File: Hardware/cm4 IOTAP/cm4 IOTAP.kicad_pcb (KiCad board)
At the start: 2 copper layers, 120 x 110 mm, 97 parts, among them IC1 TPS3700-WSON, J1 USB_C_Receptacle_USB2.0, K1 J104D2C3VDC.15S, Q1 AO3400A, U1 MAX15062A, U2 Compute_Module_4_Connectors, U3 PC817, U4 PC817, U5 PC817, U6 PC817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

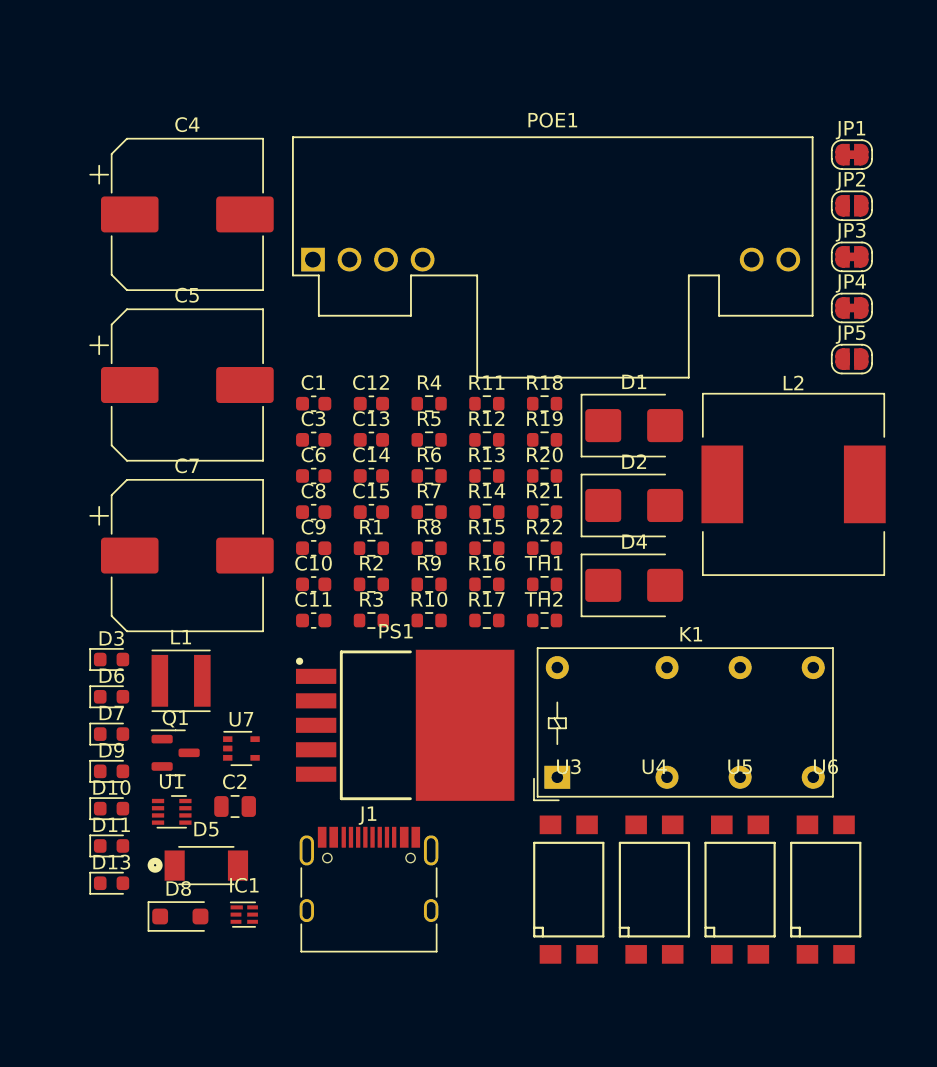
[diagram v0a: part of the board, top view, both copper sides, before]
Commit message: add resistors for Ethernet activity lights
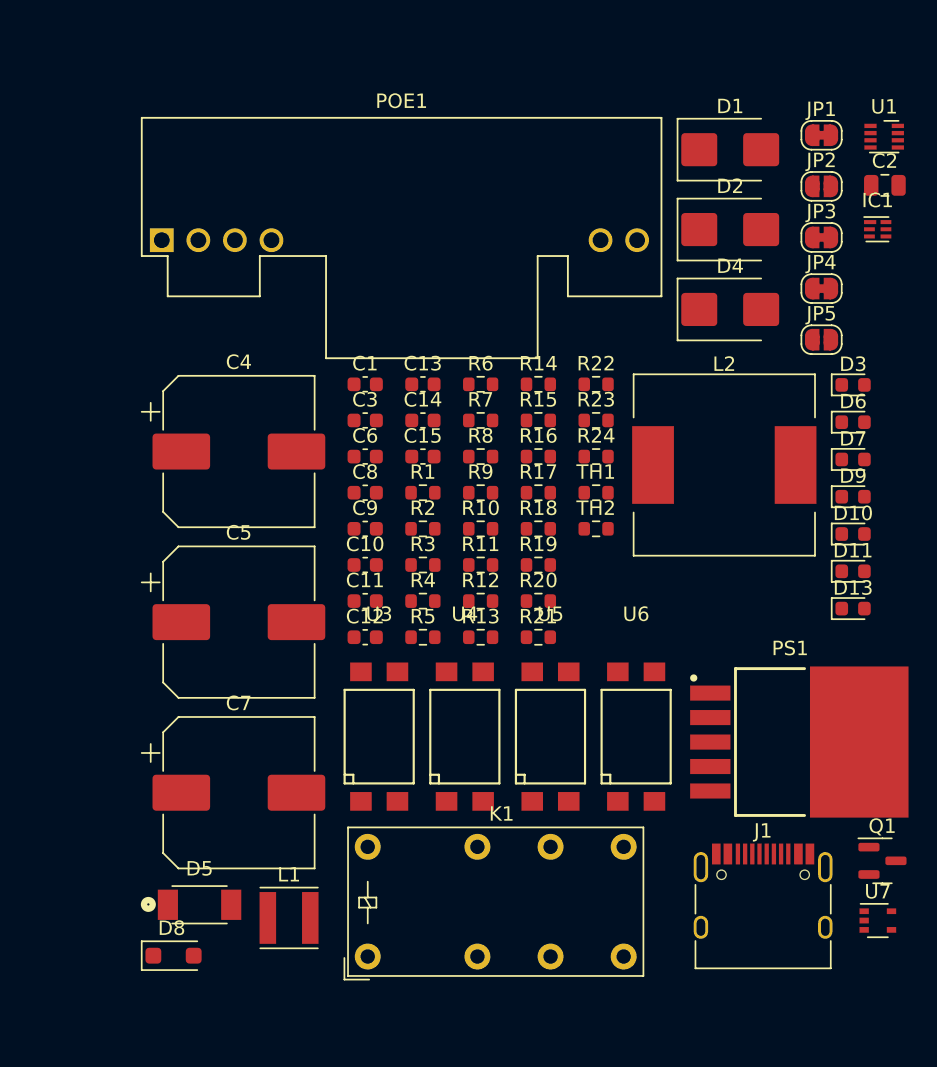
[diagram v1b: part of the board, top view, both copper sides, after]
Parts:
- added R23: 470r, Resistor_SMD:R_0603_1608Metric, F.Cu at (217.2, 49.9)
- added R24: 470r, Resistor_SMD:R_0603_1608Metric, F.Cu at (217.2, 52.4)
- moved U1 68.2 mm to (237.2, 30.2)
- moved IC1 64.8 mm to (236.7, 36.6)
- moved C2 62.4 mm to (237.2, 33.6)
- moved D10 54.9 mm to (235.0, 57.8)
- moved D11 54.9 mm to (235.0, 60.4)
- moved D13 54.9 mm to (235.0, 63.0)
- moved D3 54.9 mm to (235.0, 47.4)
- moved D6 54.9 mm to (235.0, 50.0)
- moved D7 54.9 mm to (235.0, 52.6)
- moved D9 54.9 mm to (235.0, 55.2)
- moved Q1 49.7 mm to (237.1, 80.5)
- moved U7 45.8 mm to (236.8, 84.7)
- moved J1 27.4 mm to (228.8, 84.1)
- moved PS1 27.4 mm to (230.7, 72.2)
- moved D1 20.3 mm to (226.5, 31.1)
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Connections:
- RJ45_1 pad 17: ETH_LEDY -> Net-(RJ45_1-K_YELLOW)
- RJ45_1 pad 19: ETH_LEDG -> Net-(RJ45_1-K_GREEN/A_ORANGE)
